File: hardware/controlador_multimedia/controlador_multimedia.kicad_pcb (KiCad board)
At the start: 2 copper layers, 117 x 77.5 mm, 19 parts, among them J1 Conn_01x15, J2 Conn_01x15, J3 Conn_01x06, J4 Conn_01x06, J5 Conn_01x04, J6 Conn_01x04, J7 Conn_01x03, J8 Conn_01x02, SW1 SW_Push, SW2 SW_Push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

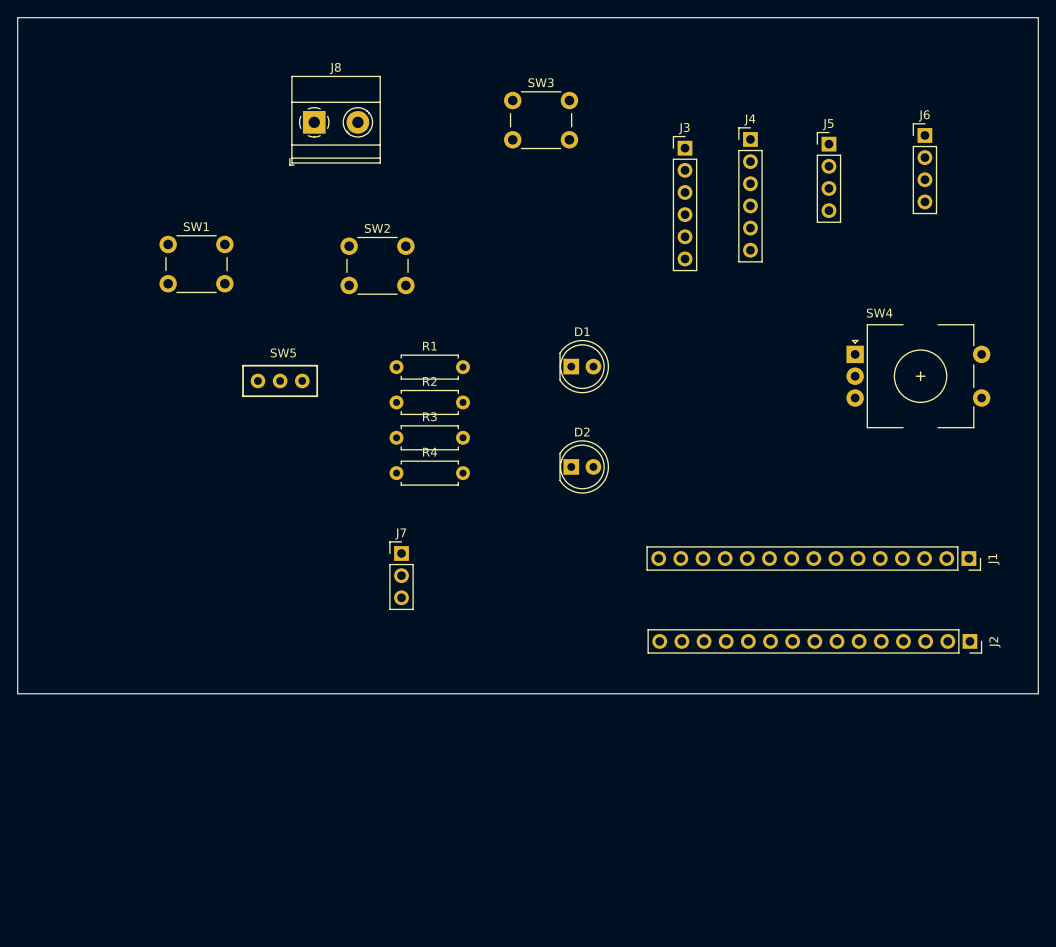
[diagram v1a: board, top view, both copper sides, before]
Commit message: hardware: agregar diseño PCB v1.0 con ruteo completo, plano GND y Gerbers
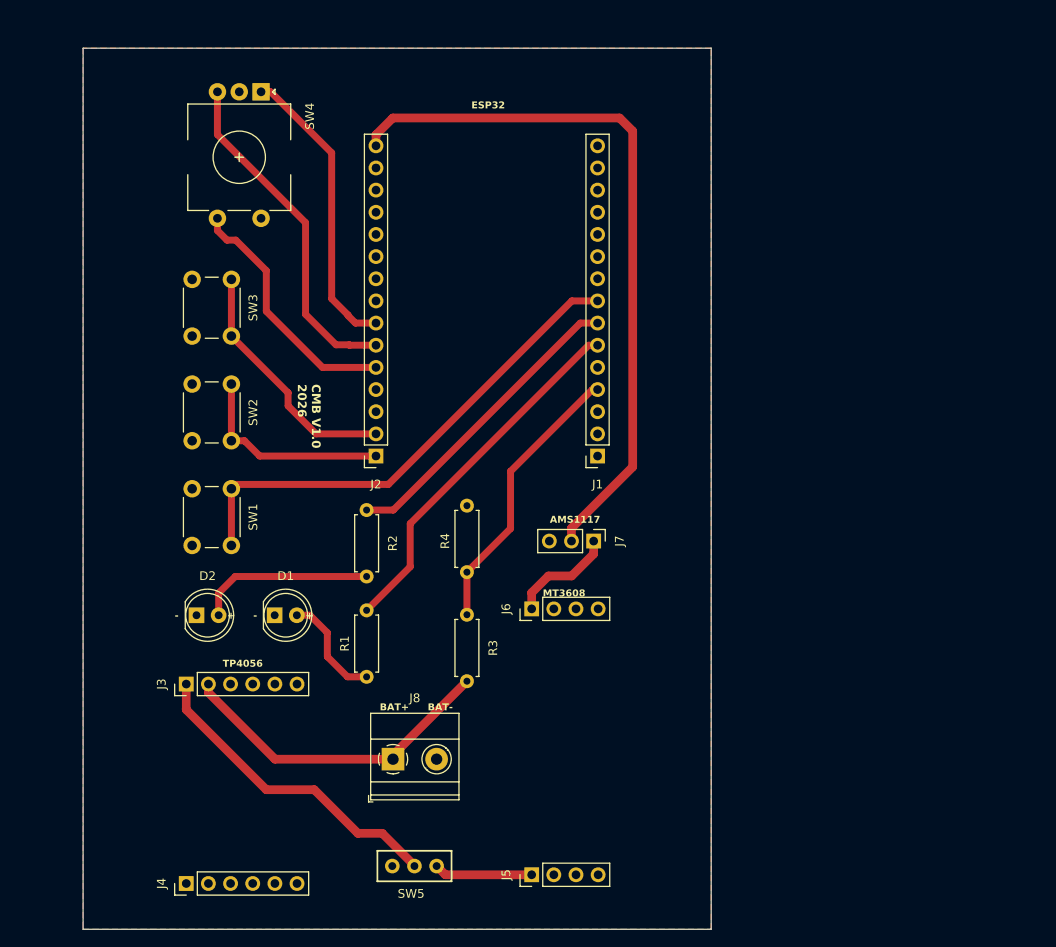
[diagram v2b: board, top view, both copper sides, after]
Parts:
- moved J4 107.0 mm to (126.8, 156.2), turned to 90 degrees
- moved J5 90.4 mm to (166.4, 155.2), turned to 90 degrees
- moved J3 83.9 mm to (126.8, 133.4), turned to 90 degrees
- moved SW4 74.5 mm to (135.4, 65.5), turned to -90 degrees
- moved J8 73.6 mm to (150.5, 142.0)
- moved J2 71.3 mm to (148.6, 107.2), turned to 180 degrees
- moved J6 70.6 mm to (166.4, 124.8), turned to 90 degrees
- moved SW5 57.7 mm to (153.0, 154.2), turned to 180 degrees
- moved D2 46.2 mm to (128.0, 125.5)
- moved D1 44.4 mm to (137.0, 125.5)
- moved J1 44.2 mm to (174.0, 107.2), turned to 180 degrees
- moved SW3 38.2 mm to (132.0, 87.0), turned to -90 degrees
- moved R1 35.7 mm to (147.5, 132.6), turned to 90 degrees
- moved SW1 28.9 mm to (132.0, 111.0), turned to -90 degrees
- moved J7 22.1 mm to (173.5, 117.0), turned to -90 degrees
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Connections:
- J1 pad 6: unconnected-(J1-Pin_6-Pad6) -> /LED_BT
- J1 pad 7: /BTN_MUTE -> /LED_BAT
- J1 pad 8: /LED_BT -> /BTN_MUTE
- J1 pad 9: /LED_BAT -> unconnected-(J1-Pin_9-Pad9)
- J3 pad 5: /BAT_N -> GND
- J3 pad 6: /OUT_N -> GND
- J5 pad 4: /OUT_N -> GND
- J8 pad 2: /BAT_N -> GND
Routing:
- net VCC: track 0.00 -> 82.0 mm
- net /BTN_MUTE: track 0.00 -> 57.4 mm
- net /LED_BT: track 0.00 -> 42.0 mm
- net /ENC_DT: track 0.00 -> 39.3 mm
- net /BAT_P: track 0.00 -> 37.7 mm
- net /OUT_P: track 0.00 -> 36.6 mm
- net /LED_BAT: track 0.00 -> 35.4 mm
- net /ENC_CLK: track 0.00 -> 34.0 mm
- net /VBAT_ADC: track 0.00 -> 32.4 mm
- net /ENC_SW: track 0.00 -> 28.8 mm
- net /BTN_PREV: track 0.00 -> 28.6 mm
- net /BTN_NEXT: track 0.00 -> 23.8 mm
- net Net-(D2-A): track 0.00 -> 20.3 mm
- net Net-(D1-A): track 0.00 -> 12.5 mm
- net /BOOST_P: track 0.00 -> 12.3 mm
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- added copper zone on F.Cu, net GND
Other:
- board size 117 x 77.5 mm -> 72 x 101 mm
- board text added: "+"
- board text added: "-"
- board text added: "AMS1117"
- board text added: "BAT+"
- board text added: "BAT-"
- board text added: "CMB V1.0 2026"
- board text added: "ESP32"
- board text added: "MT3608"
- board text added: "TP4056"
